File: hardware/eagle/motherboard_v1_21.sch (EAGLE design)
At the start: 43 parts, among them Y1 16MHz

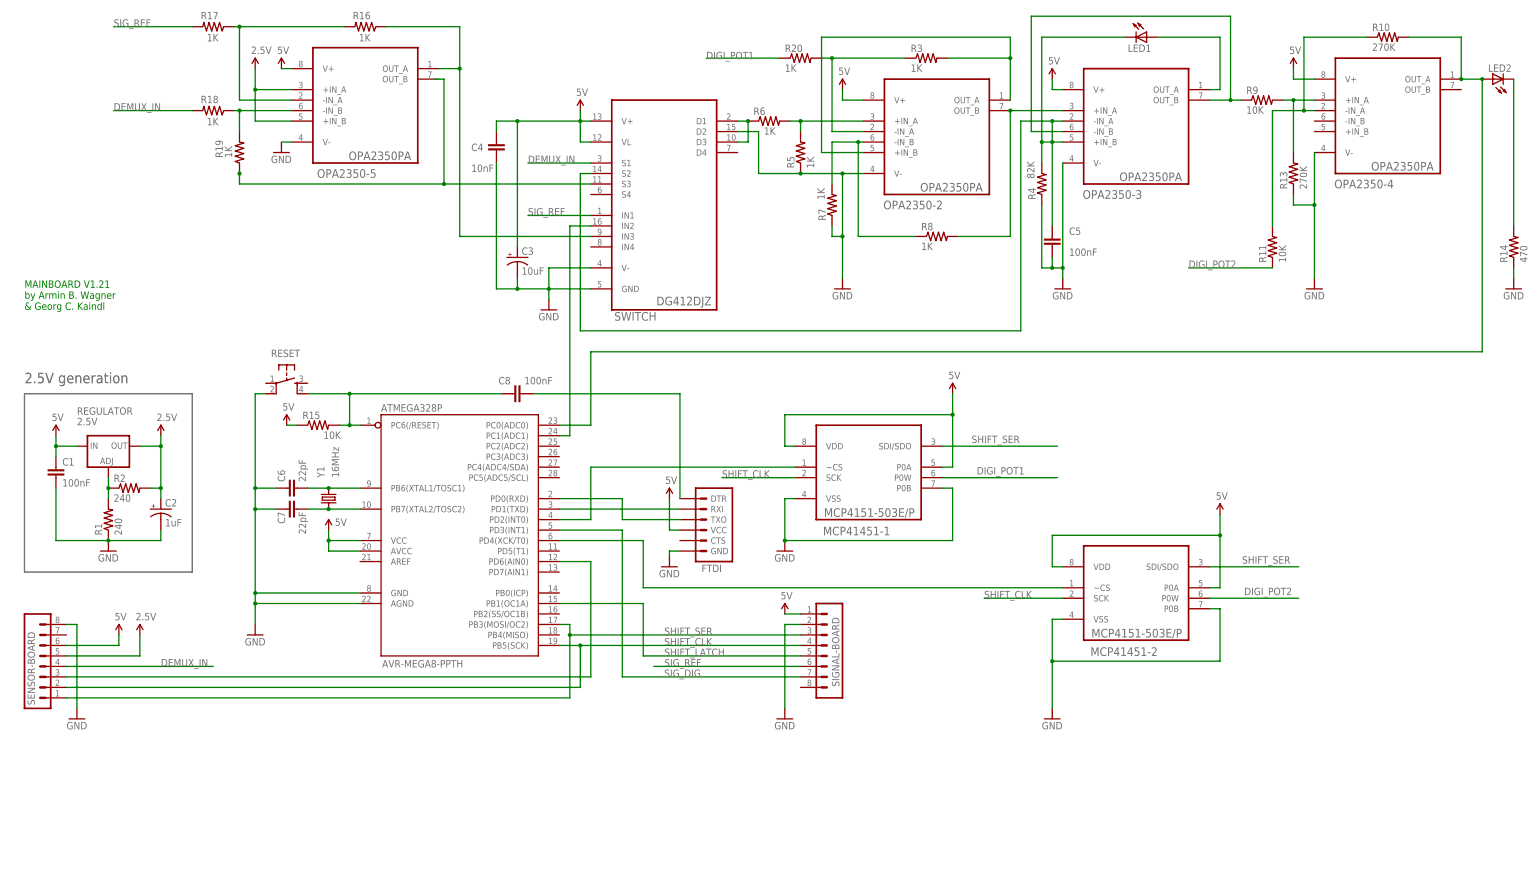
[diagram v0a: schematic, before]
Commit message: The motherboard version 1.21 includes the missing connection on the OPA2350-5. I also worked a bit on the routing and added a printout of the schematics.
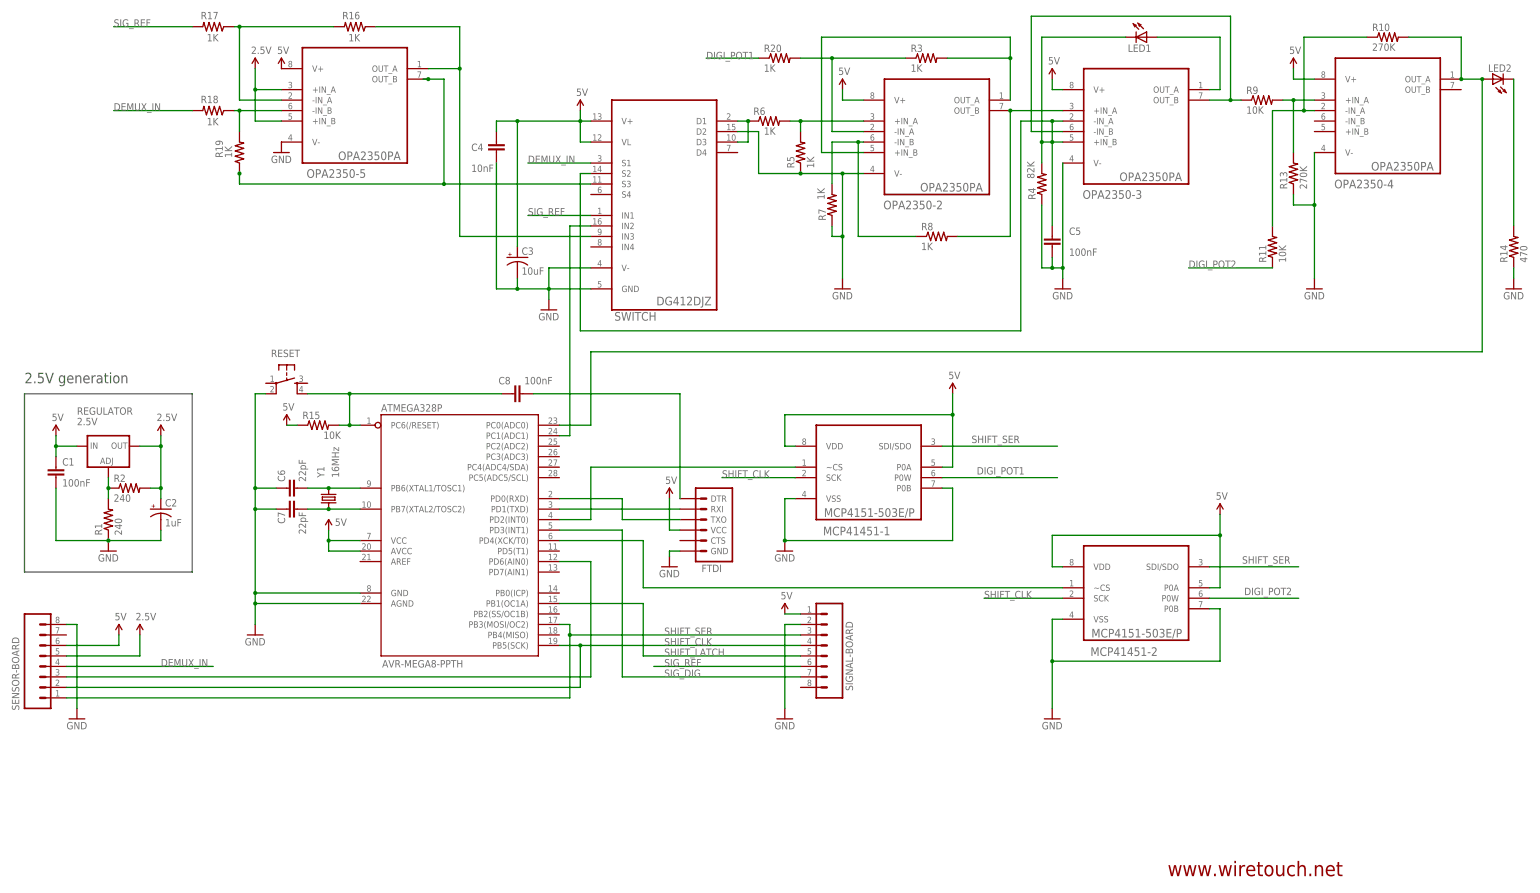
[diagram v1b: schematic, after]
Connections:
- net N$27: now also OPA2350-5.OUT_B
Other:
- note added: "www.wiretouch.net"
- note removed: "MAINBOARD V1.21 by Armin B. Wagner & Georg C. Kaindl"
- moved on the sheet: OPA2350-5, R16, R20
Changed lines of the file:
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@@
 <?xml version="1.0" encoding="utf-8"?>
 <!DOCTYPE eagle SYSTEM "eagle.dtd">
-<eagle version="7.2.0">
+<eagle version="7.5.0">
 <drawing>
 <settings>
@@
 <setting verticaltext="up"/>
 </settings>
-<grid distance="0.1" unitdist="inch" unit="inch" style="lines" multiple="1" display="no" altdistance="0.01" altunitdist="inch" altunit="inch"/>
+<grid distance="0.1" unitdist="inch" unit="inch" style="lines" multiple="1" display="no" altdistance="0.05" altunitdist="inch" altunit="inch"/>
 <layers>
 <layer number="1" name="Top" color="4" fill="1" visible="no" active="no"/>
@@
 <part name="5V5" library="SparkFun-Aesthetics" deviceset="5V" device=""/>
 <part name="RESET" library="SparkFun-Electromechanical" deviceset="TAC_SWITCH" device="PTH"/>
+<part name="FRAME1" library="frames" deviceset="A3L-LOC" device=""/>
 </parts>
 <sheets>
@@
 <wire x1="58.42" y1="-7.62" x2="58.42" y2="35.56" width="0.1524" layer="97"/>
 <wire x1="58.42" y1="35.56" x2="99.06" y2="35.56" width="0.1524" layer="97"/>
-<text x="58.42" y="55.88" size="1.778" layer="91" font="vector">MAINBOARD V1.21
-by Armin B. Wagner
-&amp; Georg C. Kaindl</text>
+<text x="335.28" y="-81.28" size="3.556" layer="94" font="vector" distance="100">www.wiretouch.net</text>
 </plain>
 <instances>
@@
 <instance part="GND9" gate="1" x="214.63" y="-6.35"/>
 <instance part="SIGNAL-BOARD" gate="G$1" x="251.46" y="-25.4" smashed="yes" rot="R180">
-<attribute name="VALUE" x="256.54" y="-12.7" size="1.778" layer="96" rot="R180"/>
-<attribute name="NAME" x="254" y="-18.542" size="1.778" layer="95" rot="R270"/>
+<attribute name="VALUE" x="255.27" y="-36.83" size="1.778" layer="96" rot="R90"/>
+<attribute name="NAME" x="257.302" y="-19.558" size="1.778" layer="95" rot="R270"/>
 </instance>
 <instance part="5V30" gate="G$1" x="242.57" y="-17.78"/>
@@
 <instance part="2.5V2" gate="G$1" x="86.36" y="-22.86"/>
 <instance part="SENSOR-BOARD" gate="G$1" x="63.5" y="-30.48" smashed="yes">
-<attribute name="VALUE" x="58.42" y="-43.18" size="1.778" layer="96"/>
-<attribute name="NAME" x="60.96" y="-39.878" size="1.778" layer="95" rot="R90"/>
-</instance>
-<instance part="OPA2350-5" gate="A" x="140.97" y="109.22" smashed="yes">
-<attribute name="NAME" x="129.2606" y="87.8586" size="2.0828" layer="95" ratio="10" rot="SR0"/>
-<attribute name="VALUE" x="136.906" y="92.1512" size="2.0828" layer="96" ratio="10" rot="SR0"/>
+<attribute name="VALUE" x="60.96" y="-39.37" size="1.778" layer="96" rot="R90"/>
+<attribute name="NAME" x="57.15" y="-41.148" size="1.778" layer="95" rot="R90"/>
+</instance>
+<instance part="OPA2350-5" gate="A" x="138.43" y="109.22" smashed="yes">
+<attribute name="NAME" x="126.7206" y="87.8586" size="2.0828" layer="95" ratio="10" rot="SR0"/>
+<attribute name="VALUE" x="134.366" y="92.1512" size="2.0828" layer="96" ratio="10" rot="SR0"/>
 </instance>
 <instance part="GND11" gate="1" x="120.65" y="93.98"/>
 <instance part="5V10" gate="G$1" x="120.65" y="114.3"/>
-<instance part="R16" gate="G$1" x="140.97" y="124.46" smashed="yes" rot="R180">
-<attribute name="NAME" x="142.24" y="128.0414" size="1.778" layer="95" rot="R180"/>
-<attribute name="VALUE" x="142.24" y="122.682" size="1.778" layer="96" rot="R180"/>
+<instance part="R16" gate="G$1" x="138.43" y="124.46" smashed="yes" rot="R180">
+<attribute name="NAME" x="139.7" y="128.0414" size="1.778" layer="95" rot="R180"/>
+<attribute name="VALUE" x="139.7" y="122.682" size="1.778" layer="96" rot="R180"/>
 </instance>
 <instance part="R17" gate="G$1" x="104.14" y="124.46" smashed="yes" rot="R180">
@@
 <attribute name="VALUE" x="108.712" y="92.71" size="1.778" layer="96" rot="R90"/>
 </instance>
-<instance part="R20" gate="G$1" x="246.38" y="116.84"/>
+<instance part="R20" gate="G$1" x="241.3" y="116.84"/>
 <instance part="MCP41451-1" gate="A" x="262.89" y="20.32" smashed="yes">
 <attribute name="NAME" x="251.8156" y="1.27" size="2.0828" layer="95" ratio="10" rot="SR0"/>
@@
 <attribute name="VALUE" x="119.38" y="31.75" size="1.778" layer="96"/>
 </instance>
+<instance part="FRAME1" gate="G$1" x="45.72" y="-86.36"/>
 </instances>
 <busses>
@@
 <pinref part="OPA2350-5" gate="A" pin="V+"/>
 <pinref part="5V10" gate="G$1" pin="5V"/>
-<wire x1="123.19" y1="114.3" x2="120.65" y2="114.3" width="0.1524" layer="91"/>
 </segment>
 <segment>
@@
 <segment>
 <pinref part="OPA2350-5" gate="A" pin="+IN_A"/>
-<wire x1="123.19" y1="109.22" x2="114.3" y2="109.22" width="0.1524" layer="91"/>
+<wire x1="120.65" y1="109.22" x2="114.3" y2="109.22" width="0.1524" layer="91"/>
 <pinref part="2.5V3" gate="G$1" pin="2.8V"/>
 <wire x1="114.3" y1="109.22" x2="114.3" y2="114.3" width="0.1524" layer="91"/>
 <wire x1="114.3" y1="109.22" x2="114.3" y2="101.6" width="0.1524" layer="91"/>
 <pinref part="OPA2350-5" gate="A" pin="+IN_B"/>
-<wire x1="114.3" y1="101.6" x2="123.19" y2="101.6" width="0.1524" layer="91"/>
+<wire x1="114.3" y1="101.6" x2="120.65" y2="101.6" width="0.1524" layer="91"/>
 <junction x="114.3" y="109.22"/>
 </segment>
@@
 <pinref part="OPA2350-5" gate="A" pin="V-"/>
 <pinref part="GND11" gate="1" pin="GND"/>
-<wire x1="123.19" y1="96.52" x2="120.65" y2="96.52" width="0.1524" layer="91"/>
 </segment>
 <segment>
@@
 <wire x1="254" y1="116.84" x2="271.78" y2="116.84" width="0.1524" layer="91"/>
 <pinref part="R20" gate="G$1" pin="2"/>
-<wire x1="254" y1="116.84" x2="251.46" y2="116.84" width="0.1524" layer="91"/>
+<wire x1="254" y1="116.84" x2="246.38" y2="116.84" width="0.1524" layer="91"/>
 <junction x="254" y="116.84"/>
 </segment>
@@
 <wire x1="163.83" y1="73.66" x2="163.83" y2="114.3" width="0.1524" layer="91"/>
 <pinref part="OPA2350-5" gate="A" pin="OUT_A"/>
-<wire x1="163.83" y1="114.3" x2="158.75" y2="114.3" width="0.1524" layer="91"/>
+<wire x1="163.83" y1="114.3" x2="156.21" y2="114.3" width="0.1524" layer="91"/>
 <wire x1="163.83" y1="114.3" x2="163.83" y2="124.46" width="0.1524" layer="91"/>
 <pinref part="R16" gate="G$1" pin="1"/>
-<wire x1="163.83" y1="124.46" x2="146.05" y2="124.46" width="0.1524" layer="91"/>
+<wire x1="163.83" y1="124.46" x2="143.51" y2="124.46" width="0.1524" layer="91"/>
 <junction x="163.83" y="114.3"/>
 </segment>
@@
 <segment>
 <pinref part="R16" gate="G$1" pin="2"/>
-<wire x1="135.89" y1="124.46" x2="110.49" y2="124.46" width="0.1524" layer="91"/>
+<wire x1="133.35" y1="124.46" x2="110.49" y2="124.46" width="0.1524" layer="91"/>
 <pinref part="R17" gate="G$1" pin="1"/>
 <pinref part="OPA2350-5" gate="A" pin="-IN_A"/>
 <wire x1="110.49" y1="124.46" x2="109.22" y2="124.46" width="0.1524" layer="91"/>
-<wire x1="123.19" y1="106.68" x2="110.49" y2="106.68" width="0.1524" layer="91"/>
+<wire x1="120.65" y1="106.68" x2="110.49" y2="106.68" width="0.1524" layer="91"/>
 <wire x1="110.49" y1="106.68" x2="110.49" y2="124.46" width="0.1524" layer="91"/>
 <junction x="110.49" y="124.46"/>
@@
 <pinref part="R19" gate="G$1" pin="1"/>
 <junction x="110.49" y="88.9"/>
+<junction x="160.02" y="86.36"/>
 <wire x1="160.02" y1="86.36" x2="195.58" y2="86.36" width="0.1524" layer="91"/>
-<wire x1="157.48" y1="111.76" x2="160.02" y2="111.76" width="0.1524" layer="91"/>
-<wire x1="160.02" y1="111.76" x2="160.02" y2="86.36" width="0.1524" layer="91"/>
-<junction x="160.02" y="86.36"/>
+<wire x1="160.02" y1="86.36" x2="160.02" y2="111.76" width="0.1524" layer="91"/>
+<wire x1="160.02" y1="111.76" x2="156.21" y2="111.76" width="0.1524" layer="91"/>
+<pinref part="OPA2350-5" gate="A" pin="OUT_B"/>
+<wire x1="156.21" y1="111.76" x2="154.94" y2="111.76" width="0.1524" layer="91"/>
+<junction x="156.21" y="111.76"/>
 </segment>
 </net>
@@
 <segment>
 <pinref part="R20" gate="G$1" pin="1"/>
-<wire x1="241.3" y1="116.84" x2="223.52" y2="116.84" width="0.1524" layer="91"/>
+<wire x1="236.22" y1="116.84" x2="223.52" y2="116.84" width="0.1524" layer="91"/>
 <label x="223.52" y="116.586" size="1.778" layer="95"/>
 </segment>
@@
 <pinref part="R18" gate="G$1" pin="1"/>
 <pinref part="OPA2350-5" gate="A" pin="-IN_B"/>
-<wire x1="123.19" y1="104.14" x2="110.49" y2="104.14" width="0.1524" layer="91"/>
+<wire x1="120.65" y1="104.14" x2="110.49" y2="104.14" width="0.1524" layer="91"/>
 <wire x1="110.49" y1="104.14" x2="109.22" y2="104.14" width="0.1524" layer="91"/>
 <pinref part="R19" gate="G$1" pin="2"/>
@@
 </sheet>
 </sheets>
+<errors>
+</errors>
 </schematic>
 </drawing>
-<compatibility>
-<note version="6.3" minversion="6.2.2" severity="warning">
-Since Version 6.2.2 text objects can contain more than one line,
-which will not be processed correctly with this version.
-</note>
-</compatibility>
 </eagle>
